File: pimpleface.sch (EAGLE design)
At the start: 29 parts, among them J1 B06B-HCMKK

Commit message: Add files via upload
Autorouted shitty board. MVP.
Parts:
- added J2, J3: POWERPOLE_POWER45A_DRILL, powerpoles:POWERPOLE_POWER45A_DRILL
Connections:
- removed net N$13: J1.6, TP8.TP
- net N$22: now also J2.V+, J3.V+
- net N$8: now also J1.6, J2.GND, J3.GND, TP8.TP
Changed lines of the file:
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@@
 <part name="D3" library="diode" library_urn="urn:adsk.eagle:library:210" deviceset="BYV95" device="" package3d_urn="urn:adsk.eagle:package:43367/1"/>
 <part name="R3" library="rcl" library_urn="urn:adsk.eagle:library:334" deviceset="R-US_" device="R0805" package3d_urn="urn:adsk.eagle:package:23553/2"/>
+<part name="J2" library="powerpoles" deviceset="POWERPOLE_POWER" device="45A_DRILL"/>
+<part name="J3" library="powerpoles" deviceset="POWERPOLE_POWER" device="45A_DRILL"/>
 </parts>
 <sheets>
@@
 <attribute name="VALUE" x="64.262" y="16.51" size="1.778" layer="96" rot="R90"/>
 </instance>
+<instance part="J2" gate="G$1" x="106.68" y="15.24" smashed="yes"/>
+<instance part="J3" gate="G$1" x="106.68" y="-5.08" smashed="yes"/>
 </instances>
 <busses>
@@
 <pinref part="C4" gate="G$1" pin="2"/>
 <wire x1="88.9" y1="5.08" x2="88.9" y2="-2.54" width="0.1524" layer="91"/>
-<wire x1="88.9" y1="-2.54" x2="88.9" y2="-12.7" width="0.1524" layer="91"/>
+<wire x1="88.9" y1="-2.54" x2="88.9" y2="-10.16" width="0.1524" layer="91"/>
+<wire x1="88.9" y1="-10.16" x2="88.9" y2="-12.7" width="0.1524" layer="91"/>
 <wire x1="88.9" y1="-12.7" x2="76.2" y2="-12.7" width="0.1524" layer="91"/>
 <wire x1="91.44" y1="5.08" x2="88.9" y2="5.08" width="0.1524" layer="91"/>
 <junction x="88.9" y="5.08"/>
-<wire x1="91.44" y1="7.62" x2="91.44" y2="5.08" width="0.1524" layer="91"/>
 <pinref part="TP11" gate="G$1" pin="TP"/>
 <junction x="88.9" y="-2.54"/>
+<pinref part="J1" gate="G$1" pin="6"/>
+<wire x1="91.44" y1="50.8" x2="91.44" y2="35.56" width="0.1524" layer="91"/>
+<pinref part="TP8" gate="G$1" pin="TP"/>
+<wire x1="91.44" y1="35.56" x2="91.44" y2="10.16" width="0.1524" layer="91"/>
+<junction x="91.44" y="35.56"/>
+<pinref part="J2" gate="G$1" pin="GND"/>
+<wire x1="91.44" y1="10.16" x2="91.44" y2="5.08" width="0.1524" layer="91"/>
+<wire x1="96.52" y1="10.16" x2="91.44" y2="10.16" width="0.1524" layer="91"/>
+<junction x="91.44" y="10.16"/>
+<pinref part="J3" gate="G$1" pin="GND"/>
+<wire x1="96.52" y1="-10.16" x2="88.9" y2="-10.16" width="0.1524" layer="91"/>
+<junction x="88.9" y="-10.16"/>
 </segment>
 </net>
@@
 </segment>
 </net>
-<net name="N$13" class="0">
-<segment>
-<pinref part="J1" gate="G$1" pin="6"/>
-<wire x1="91.44" y1="50.8" x2="91.44" y2="35.56" width="0.1524" layer="91"/>
-<pinref part="TP8" gate="G$1" pin="TP"/>
-<wire x1="91.44" y1="35.56" x2="91.44" y2="7.62" width="0.1524" layer="91"/>
-<junction x="91.44" y="35.56"/>
-</segment>
-</net>
 <net name="N$22" class="0">
 <segment>
@@
 <junction x="63.5" y="55.88"/>
 <wire x1="60.96" y1="55.88" x2="63.5" y2="55.88" width="0.1524" layer="91"/>
-<wire x1="60.96" y1="38.1" x2="60.96" y2="55.88" width="0.1524" layer="91"/>
+<wire x1="60.96" y1="38.1" x2="60.96" y2="40.64" width="0.1524" layer="91"/>
 <pinref part="D3" gate="1" pin="C"/>
-</segment>
-</net>
+<pinref part="J2" gate="G$1" pin="V+"/>
+<wire x1="60.96" y1="40.64" x2="60.96" y2="55.88" width="0.1524" layer="91"/>
+<wire x1="96.52" y1="20.32" x2="96.52" y2="33.02" width="0.1524" layer="91"/>
+<wire x1="96.52" y1="33.02" x2="96.52" y2="40.64" width="0.1524" layer="91"/>
+<wire x1="96.52" y1="40.64" x2="60.96" y2="40.64" width="0.1524" layer="91"/>
+<junction x="60.96" y="40.64"/>
+<pinref part="J3" gate="G$1" pin="V+"/>
+<wire x1="96.52" y1="0" x2="93.98" y2="0" width="0.1524" layer="91"/>
+<wire x1="93.98" y1="0" x2="93.98" y2="33.02" width="0.1524" layer="91"/>
+<wire x1="93.98" y1="33.02" x2="96.52" y2="33.02" width="0.1524" layer="91"/>
+<junction x="96.52" y="33.02"/>
+</segment>
+</net>

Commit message: Add files via upload
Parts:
- removed D1, D3: BYV95, diode:BYV95
- added LED1, LED2: (no value), led:LEDCHIP-LED0603
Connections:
- net JIMGND renamed 6AGND
- net N$8 renamed 1.6AGND
- removed net N$22: D3.C, J1.1, J2.V+, J3.V+, TP4.TP
- removed net N$34: D3.A, R3.2
- removed net N$4: D1.A, R1.2
- new net 1.6AOUT: J1.1, J2.V+, J3.V+, LED1.C, R3.2, TP4.TP
- net LED: now also LED2.C, R1.2; no longer D1.C
- net N$1: now also LED2.A
- net N$9: now also LED1.A
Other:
- moved on the sheet: R1, R3

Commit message: Add files via upload
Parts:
- removed C7: 10uF, rcl:C-USC0805
- added C1: 10uF, rcl:EL-BI25-10AXIAL
- F1: value 7.5A -> FUSESHK20L; device special:FUSE -> fuse:FUSESHK20L
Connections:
- net N$2 renamed TP-12
- net N$5 renamed TP13
- net N$6 renamed FUSE
- net 6AGND: now also C1.2; no longer C7.2
- net N$1: now also C1.1; no longer C7.1
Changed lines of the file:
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@@
 <parts>
 <part name="U$1" library="12v6aBuckConverter" deviceset="12V6ABUCKCONVERTER" device=""/>
-<part name="F1" library="special" library_urn="urn:adsk.eagle:library:367" deviceset="FUSE" device="" package3d_urn="urn:adsk.eagle:package:26650/1" value="7.5A"/>
 <part name="U$2" library="REV BLDC" deviceset="SB50" device=""/>
 <part name="J1" library="B06B-HCMKK" deviceset="B06B-HCMKK" device=""/>
@@
 <part name="U$3" library="buck_1.6" deviceset="BUCK1.6A" device=""/>
 <part name="C6" library="rcl" library_urn="urn:adsk.eagle:library:334" deviceset="C-US" device="C0805" package3d_urn="urn:adsk.eagle:package:23617/2" value="66uF"/>
-<part name="C7" library="rcl" library_urn="urn:adsk.eagle:library:334" deviceset="C-US" device="C0805" package3d_urn="urn:adsk.eagle:package:23617/2" value="10uF"/>
 <part name="TP1" library="testpad" library_urn="urn:adsk.eagle:library:385" deviceset="TP" device="PAD1-13" package3d_urn="urn:adsk.eagle:package:27946/1"/>
 <part name="TP2" library="testpad" library_urn="urn:adsk.eagle:library:385" deviceset="TP" device="PAD1-13" package3d_urn="urn:adsk.eagle:package:27946/1"/>
@@
 <part name="R3" library="rcl" library_urn="urn:adsk.eagle:library:334" deviceset="R-US_" device="R0805" package3d_urn="urn:adsk.eagle:package:23553/2"/>
 <part name="LED1" library="led" library_urn="urn:adsk.eagle:library:259" deviceset="LED" device="CHIP-LED0603" package3d_urn="urn:adsk.eagle:package:15819/3"/>
+<part name="F1" library="fuse" library_urn="urn:adsk.eagle:library:233" deviceset="FUSE" device="SHK20L" package3d_urn="urn:adsk.eagle:package:14071/1"/>
+<part name="C1" library="rcl" library_urn="urn:adsk.eagle:library:334" deviceset="EL-" device="BI25-10AXIAL" package3d_urn="urn:adsk.eagle:package:23718/1" value="10uF"/>
 </parts>
 <sheets>
@@
 <instances>
 <instance part="U$1" gate="G$1" x="45.72" y="48.26" smashed="yes"/>
-<instance part="F1" gate="G$1" x="7.62" y="63.5" smashed="yes">
-<attribute name="NAME" x="2.54" y="66.04" size="1.778" layer="95"/>
-<attribute name="VALUE" x="2.54" y="59.69" size="1.778" layer="96"/>
-</instance>
 <instance part="U$2" gate="G$1" x="-10.16" y="58.42" smashed="yes" rot="MR0"/>
 <instance part="J1" gate="G$1" x="71.12" y="55.88" smashed="yes">
@@
 <attribute name="VALUE" x="13.716" y="56.769" size="1.778" layer="96"/>
 </instance>
-<instance part="C7" gate="G$1" x="55.88" y="53.34" smashed="yes">
-<attribute name="NAME" x="56.896" y="53.975" size="1.778" layer="95"/>
-<attribute name="VALUE" x="56.896" y="49.149" size="1.778" layer="96"/>
-</instance>
 <instance part="TP1" gate="G$1" x="15.24" y="66.04" smashed="yes">
 <attribute name="NAME" x="13.97" y="67.31" size="1.778" layer="95"/>
@@
 <attribute name="NAME" x="57.404" y="37.592" size="1.778" layer="95" rot="R270"/>
 <attribute name="VALUE" x="55.245" y="37.592" size="1.778" layer="96" rot="R270"/>
+</instance>
+<instance part="F1" gate="G$1" x="5.08" y="63.5" smashed="yes">
+<attribute name="NAME" x="1.27" y="64.897" size="1.778" layer="95"/>
+<attribute name="VALUE" x="1.27" y="60.579" size="1.778" layer="96"/>
+</instance>
+<instance part="C1" gate="G$1" x="55.88" y="53.34" smashed="yes">
+<attribute name="NAME" x="57.404" y="53.721" size="1.778" layer="95"/>
+<attribute name="VALUE" x="57.404" y="48.641" size="1.778" layer="96"/>
 </instance>
 </instances>
@@
 <wire x1="71.12" y1="43.18" x2="71.12" y2="50.8" width="0.1524" layer="91"/>
 <label x="60.96" y="43.18" size="1.778" layer="95"/>
-<pinref part="C7" gate="G$1" pin="2"/>
 <pinref part="TP5" gate="G$1" pin="TP"/>
 <junction x="66.04" y="43.18"/>
+<pinref part="C1" gate="G$1" pin="2"/>
 </segment>
 </net>
 <net name="N$3" class="0">
 <segment>
-<pinref part="F1" gate="G$1" pin="2"/>
 <pinref part="U$1" gate="G$1" pin="+VIN"/>
-<wire x1="12.7" y1="63.5" x2="15.24" y2="63.5" width="0.1524" layer="91"/>
 <wire x1="15.24" y1="63.5" x2="17.78" y2="63.5" width="0.1524" layer="91"/>
 <pinref part="BUCK150UH" gate="G$1" pin="1"/>
@@
 <junction x="17.78" y="63.5"/>
 <pinref part="TP1" gate="G$1" pin="TP"/>
+<pinref part="F1" gate="G$1" pin="2"/>
+<wire x1="10.16" y1="63.5" x2="15.24" y2="63.5" width="0.1524" layer="91"/>
 </segment>
 </net>
@@
 </segment>
 </net>
-<net name="N$6" class="0">
+<net name="FUSE" class="0">
 <segment>
 <pinref part="U$2" gate="G$1" pin="+"/>
+<wire x1="-2.54" y1="63.5" x2="0" y2="63.5" width="0.1524" layer="91"/>
 <pinref part="F1" gate="G$1" pin="1"/>
-<wire x1="-2.54" y1="63.5" x2="0" y2="63.5" width="0.1524" layer="91"/>
+<label x="0" y="68.58" size="1.778" layer="95"/>
 </segment>
 </net>
@@
 <junction x="45.72" y="63.5"/>
 <wire x1="45.72" y1="63.5" x2="45.72" y2="58.42" width="0.1524" layer="91"/>
-<pinref part="C7" gate="G$1" pin="1"/>
 <pinref part="TP3" gate="G$1" pin="TP"/>
 <wire x1="55.88" y1="63.5" x2="66.04" y2="63.5" width="0.1524" layer="91"/>
@@
 <wire x1="66.04" y1="60.96" x2="66.04" y2="63.5" width="0.1524" layer="91"/>
 <junction x="66.04" y="63.5"/>
-</segment>
-</net>
-<net name="N$2" class="0">
+<pinref part="C1" gate="G$1" pin="1"/>
+</segment>
+</net>
+<net name="TP-12" class="0">
 <segment>
 <pinref part="U$4" gate="G$1" pin="1"/>
@@
 </segment>
 </net>
-<net name="N$5" class="0">
+<net name="TP13" class="0">
 <segment>
 <pinref part="BUCK150UH" gate="G$1" pin="3"/>
@@
 <pinref part="TP13" gate="G$1" pin="TP"/>
 <junction x="17.78" y="0"/>
-</segment>
-</net>
+<label x="17.78" y="-5.08" size="1.778" layer="95"/>
+</segment>
+</net>

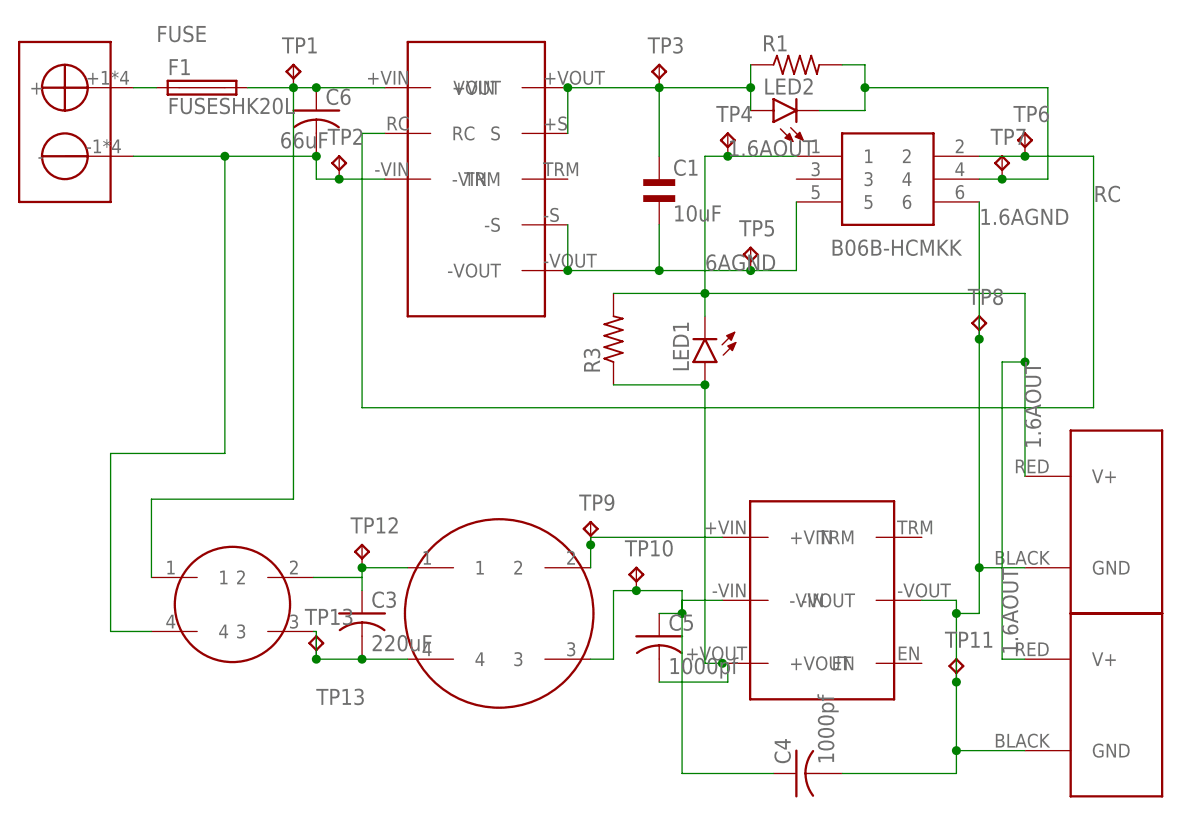
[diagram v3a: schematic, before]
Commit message: Add files via upload
Made new board and minor clean up of schematic. Still needs the LED fixed.
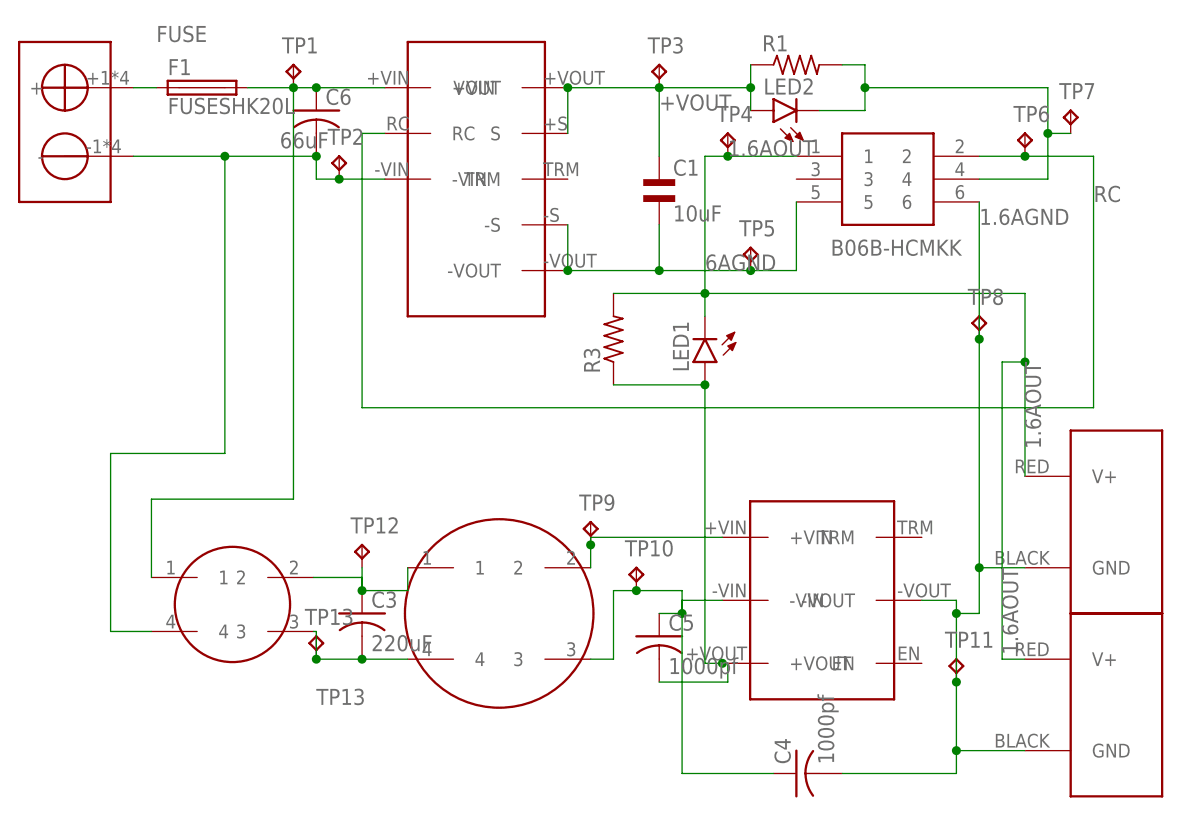
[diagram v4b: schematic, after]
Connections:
- net N$1 renamed +VOUT
- net TP-12 renamed N$24
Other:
- moved on the sheet: TP7
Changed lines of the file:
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@@
 <?xml version="1.0" encoding="utf-8"?>
 <!DOCTYPE eagle SYSTEM "eagle.dtd">
-<eagle version="9.5.0">
+<eagle version="9.5.1">
 <drawing>
 <settings>
@@
 <attribute name="TP_SIGNAL_NAME" x="97.79" y="57.15" size="1.778" layer="97"/>
 </instance>
-<instance part="TP7" gate="G$1" x="93.98" y="55.88" smashed="yes">
-<attribute name="NAME" x="92.71" y="57.15" size="1.778" layer="95"/>
-<attribute name="TP_SIGNAL_NAME" x="95.25" y="54.61" size="1.778" layer="97"/>
+<instance part="TP7" gate="G$1" x="101.6" y="60.96" smashed="yes">
+<attribute name="NAME" x="100.33" y="62.23" size="1.778" layer="95"/>
+<attribute name="TP_SIGNAL_NAME" x="102.87" y="59.69" size="1.778" layer="97"/>
 </instance>
 <instance part="TP8" gate="G$1" x="91.44" y="38.1" smashed="yes">
@@
 <net name="LED" class="0">
 <segment>
-<pinref part="J1" gate="G$1" pin="4"/>
-<wire x1="99.06" y1="63.5" x2="99.06" y2="53.34" width="0.1524" layer="91"/>
-<wire x1="99.06" y1="53.34" x2="93.98" y2="53.34" width="0.1524" layer="91"/>
-<wire x1="93.98" y1="53.34" x2="91.44" y2="53.34" width="0.1524" layer="91"/>
 <wire x1="78.74" y1="63.5" x2="99.06" y2="63.5" width="0.1524" layer="91"/>
-<pinref part="TP7" gate="G$1" pin="TP"/>
-<junction x="93.98" y="53.34"/>
 <pinref part="LED2" gate="G$1" pin="C"/>
 <wire x1="73.66" y1="60.96" x2="78.74" y2="60.96" width="0.1524" layer="91"/>
@@
 <wire x1="78.74" y1="66.04" x2="78.74" y2="63.5" width="0.1524" layer="91"/>
 <junction x="78.74" y="63.5"/>
+<pinref part="J1" gate="G$1" pin="4"/>
+<wire x1="91.44" y1="53.34" x2="99.06" y2="53.34" width="0.1524" layer="91"/>
+<wire x1="99.06" y1="53.34" x2="99.06" y2="58.42" width="0.1524" layer="91"/>
+<pinref part="TP7" gate="G$1" pin="TP"/>
+<wire x1="99.06" y1="58.42" x2="99.06" y2="63.5" width="0.1524" layer="91"/>
+<wire x1="101.6" y1="58.42" x2="99.06" y2="58.42" width="0.1524" layer="91"/>
+<junction x="99.06" y="58.42"/>
 </segment>
 </net>
@@
 </segment>
 </net>
-<net name="N$1" class="0">
+<net name="+VOUT" class="0">
 <segment>
 <pinref part="U$1" gate="G$1" pin="S"/>
@@
 <junction x="66.04" y="63.5"/>
 <pinref part="C1" gate="G$1" pin="1"/>
-</segment>
-</net>
-<net name="TP-12" class="0">
-<segment>
-<pinref part="U$4" gate="G$1" pin="1"/>
-<pinref part="C3" gate="G$1" pin="1"/>
-<wire x1="27.94" y1="10.16" x2="22.86" y2="10.16" width="0.1524" layer="91"/>
-<wire x1="22.86" y1="9.08" x2="22.86" y2="7.62" width="0.1524" layer="91"/>
-<pinref part="BUCK150UH" gate="G$1" pin="2"/>
-<wire x1="17.46" y1="9.08" x2="22.86" y2="9.08" width="0.1524" layer="91"/>
-<wire x1="22.86" y1="9.08" x2="22.86" y2="10.16" width="0.1524" layer="91"/>
-<pinref part="TP12" gate="G$1" pin="TP"/>
-<junction x="22.86" y="10.16"/>
+<label x="55.88" y="60.96" size="1.778" layer="95"/>
 </segment>
 </net>
@@
 </segment>
 </net>
+<net name="N$24" class="0">
+<segment>
+<pinref part="BUCK150UH" gate="G$1" pin="2"/>
+<pinref part="C3" gate="G$1" pin="1"/>
+<wire x1="17.46" y1="9.08" x2="22.86" y2="9.08" width="0.1524" layer="91"/>
+<wire x1="22.86" y1="9.08" x2="22.86" y2="7.62" width="0.1524" layer="91"/>
+<pinref part="U$4" gate="G$1" pin="1"/>
+<wire x1="27.94" y1="10.16" x2="27.94" y2="7.62" width="0.1524" layer="91"/>
+<wire x1="27.94" y1="7.62" x2="22.86" y2="7.62" width="0.1524" layer="91"/>
+<junction x="22.86" y="7.62"/>
+<pinref part="TP12" gate="G$1" pin="TP"/>
+<wire x1="22.86" y1="10.16" x2="22.86" y2="7.62" width="0.1524" layer="91"/>
+</segment>
+</net>
